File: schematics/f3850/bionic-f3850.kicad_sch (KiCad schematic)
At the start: 8 parts, among them J1 Bionic-P135, J2 Bionic-P245, U1 F3850, U3 LM78L12, U4 11AA010-I/TO

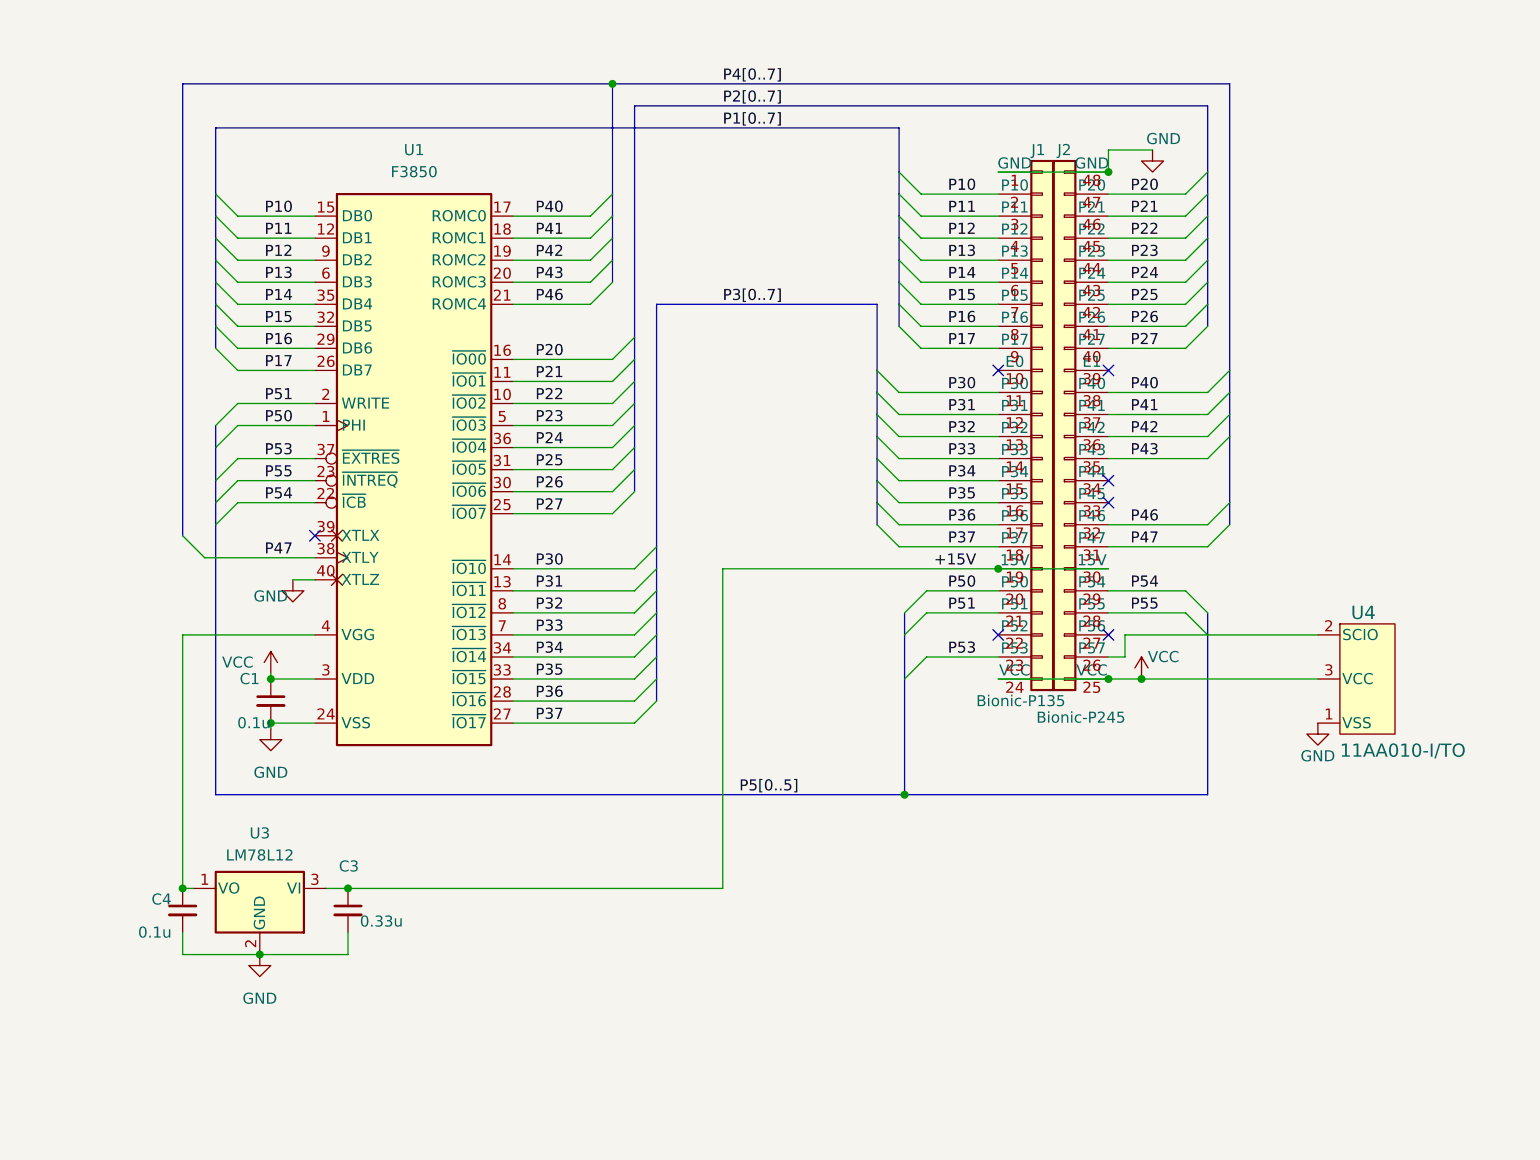
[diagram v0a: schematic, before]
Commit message: [F3850] Add power LED
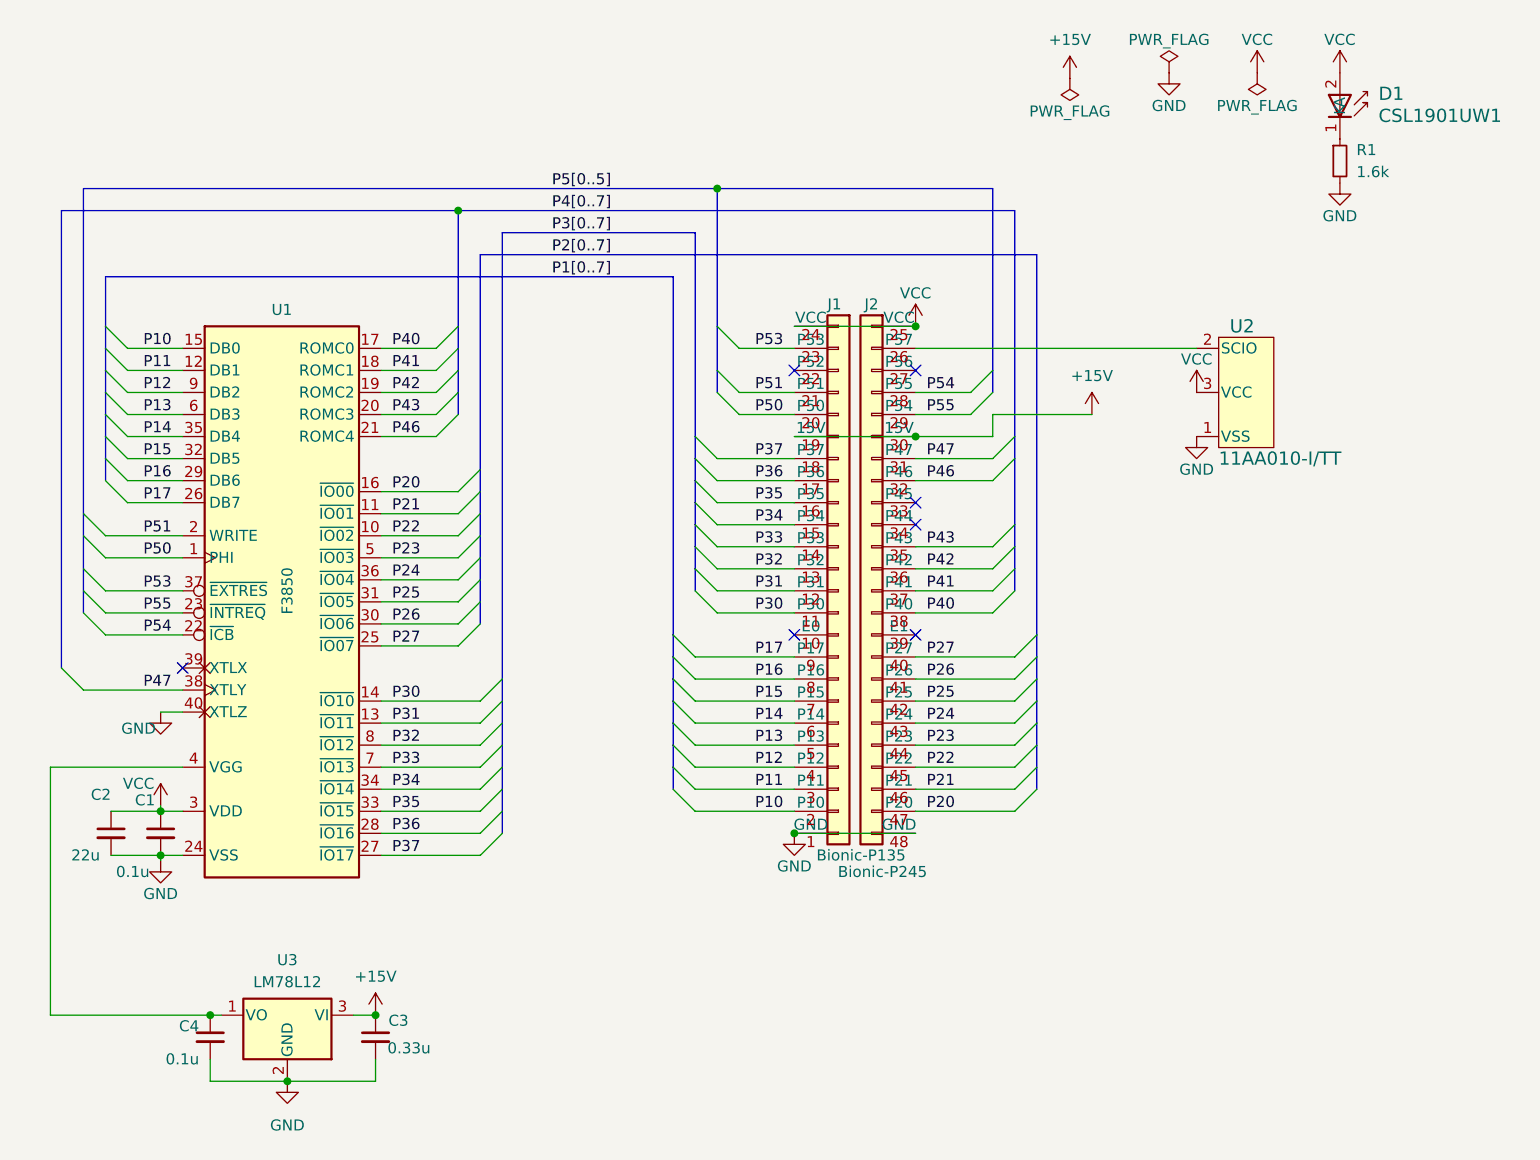
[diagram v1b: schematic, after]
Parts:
- removed U4: 11AA010-I/TO, TO-92_MC_MCH, symbol 0-LocalLibrary:11AA010-I_TO
- added C2: 22u, Capacitor_SMD:C_0603_1608Metric_Pad1.08x0.95mm_HandSolder, symbol Device:C_Small
- added D1: CSL1901UW1, 0-LocalLibrary:LED_CSL1901UW1_ROM, symbol 0-LocalLibrary:CSL1901UW1
- added R1: 1.6k, Resistor_SMD:R_0603_1608Metric_Pad0.98x0.95mm_HandSolder, symbol Device:R_Small
- added U2: 11AA010-I/TT, 0-LocalLibrary:SOT-23_MC_MCH-M, symbol 0-LocalLibrary:11AA010-I_TT
- C1, C4: footprint Capacitor_THT:C_Disc_D3.4mm_W2.1mm_P2.50mm -> Capacitor_SMD:C_0603_1608Metric_Pad1.08x0.95mm_HandSolder
- C3: footprint Capacitor_THT:C_Disc_D3.4mm_W2.1mm_P2.50mm -> Capacitor_SMD:C_1206_3216Metric_Pad1.33x1.80mm_HandSolder
- J1: footprint connector:Bionic-P135_Vertical -> 0-LocalLibrary:Bionic-P135_Vertical
- J2: footprint connector:Bionic-P245_Vertical -> 0-LocalLibrary:Bionic-P245_Vertical
- U1: footprint Package_DIP:DIP-40_W15.24mm -> 0-LocalLibrary:DIP-40_W15.24mm_Socket
- U3: footprint Package_TO_SOT_THT:TO-92_Inline -> 0-LocalLibrary:SOT-89-3_Handsoldering
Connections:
- net GND: now also C2.2, R1.2, U2.1 (VSS)
- net P54: now also J2.28 (P55); no longer J2.29 (P54)
- net P55: now also J2.29 (P54); no longer J2.28 (P55)
- net VCC: now also C2.1, D1.2 (A), U2.3 (VCC)
- net at J2.26 (P57): now also U2.2 (SCIO)
- new net: D1.1 (K), R1.1
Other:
- moved on the sheet: C1, C3, C4, U1, U3

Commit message: [F3850] Fix EEPROM pinout
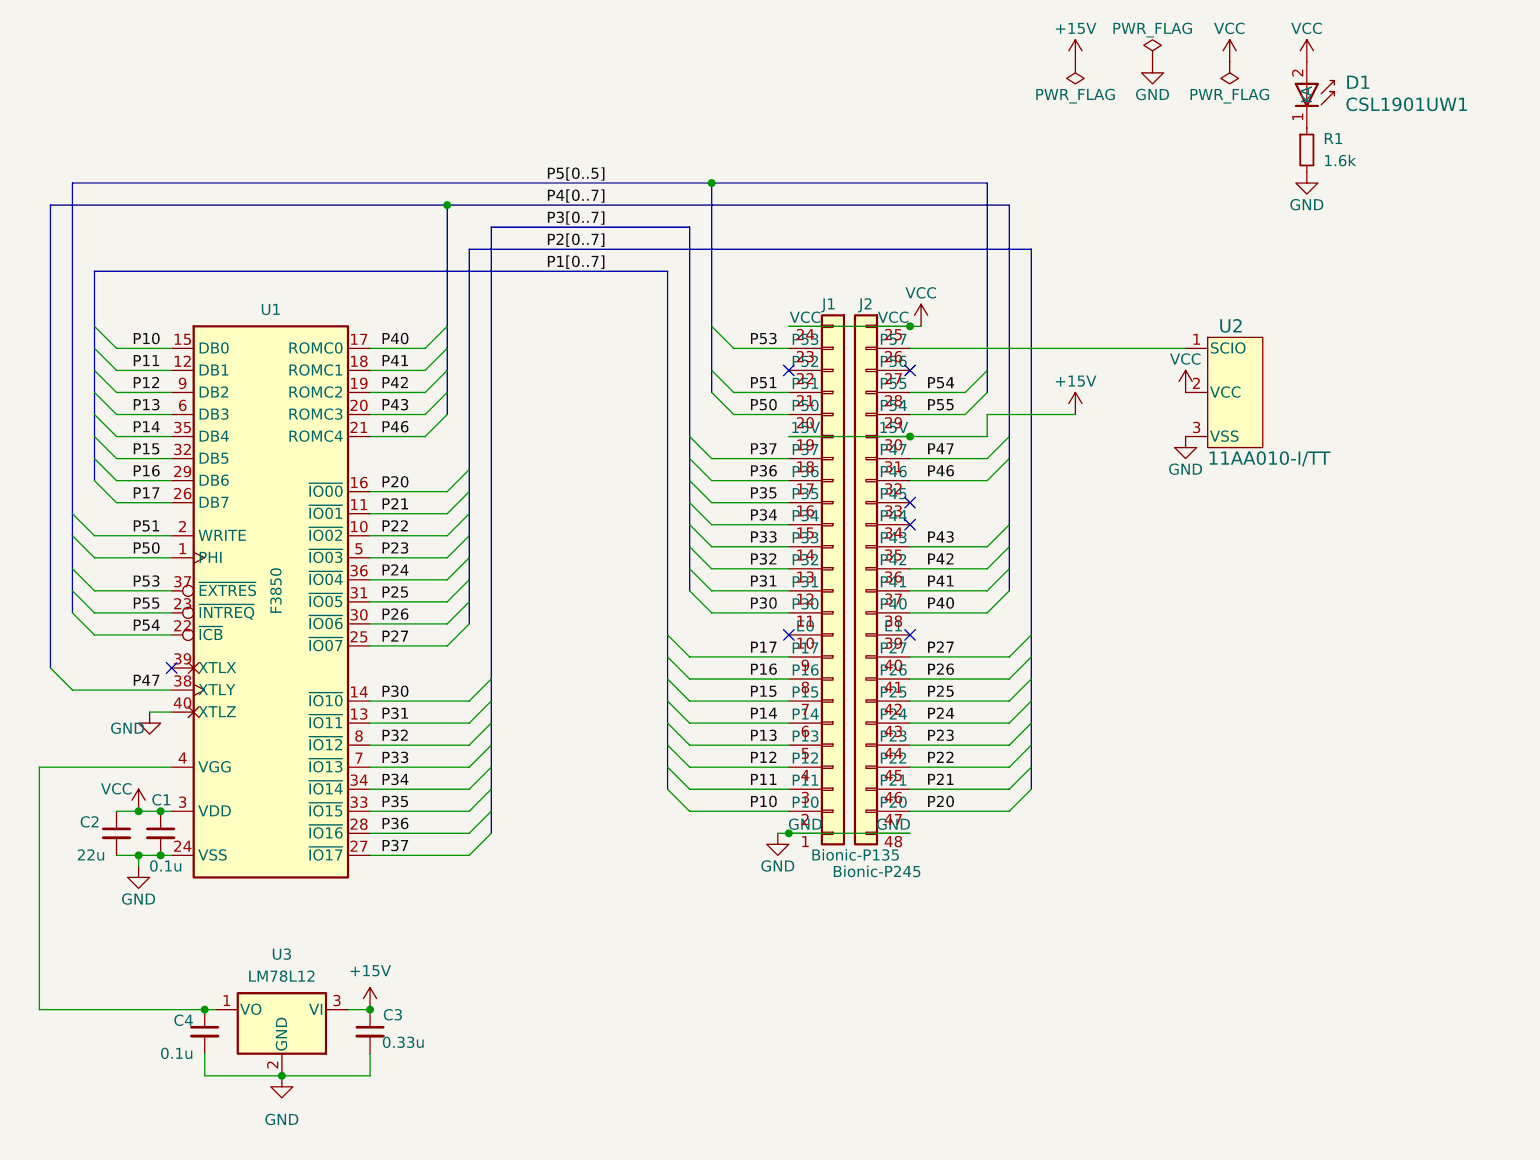
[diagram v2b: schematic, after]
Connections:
- net GND: now also U2.3 (VSS); no longer U2.1 (VSS)
- net VCC: now also U2.2 (VCC); no longer U2.3 (VCC)
- net at J2.26 (P57): now also U2.1 (SCIO); no longer U2.2 (SCIO)
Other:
- moved on the sheet: C2, C3, C4, D1, J1, J2, R1, U1, U2, U3

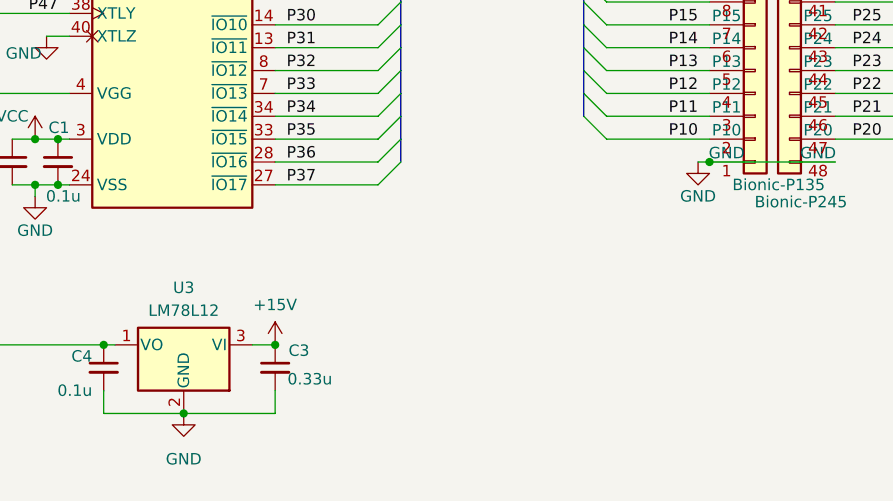
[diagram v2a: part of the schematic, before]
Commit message: [schematics] Update LED footprint
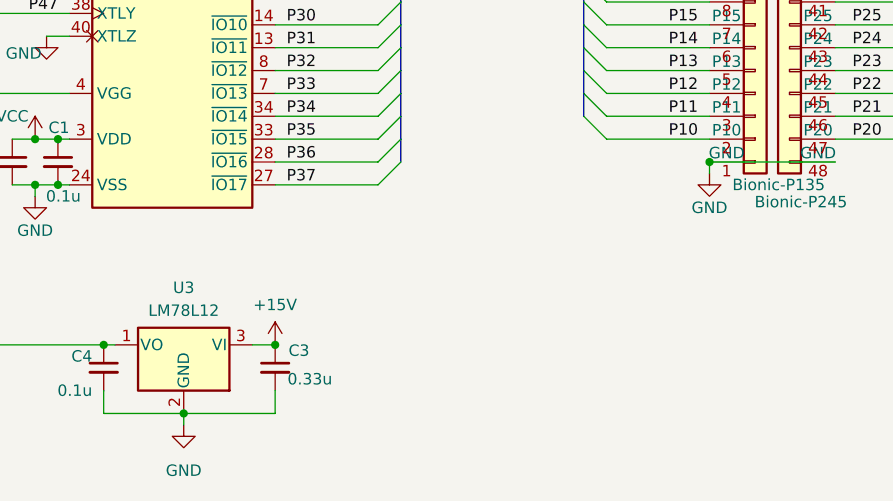
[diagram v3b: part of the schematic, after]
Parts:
- D1: footprint 0-LocalLibrary:LED_CSL1901UW1_ROM -> 0-LocalLibrary:LED_CSL1901UW1_ROM-M
